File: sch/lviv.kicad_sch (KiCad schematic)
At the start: 0 parts

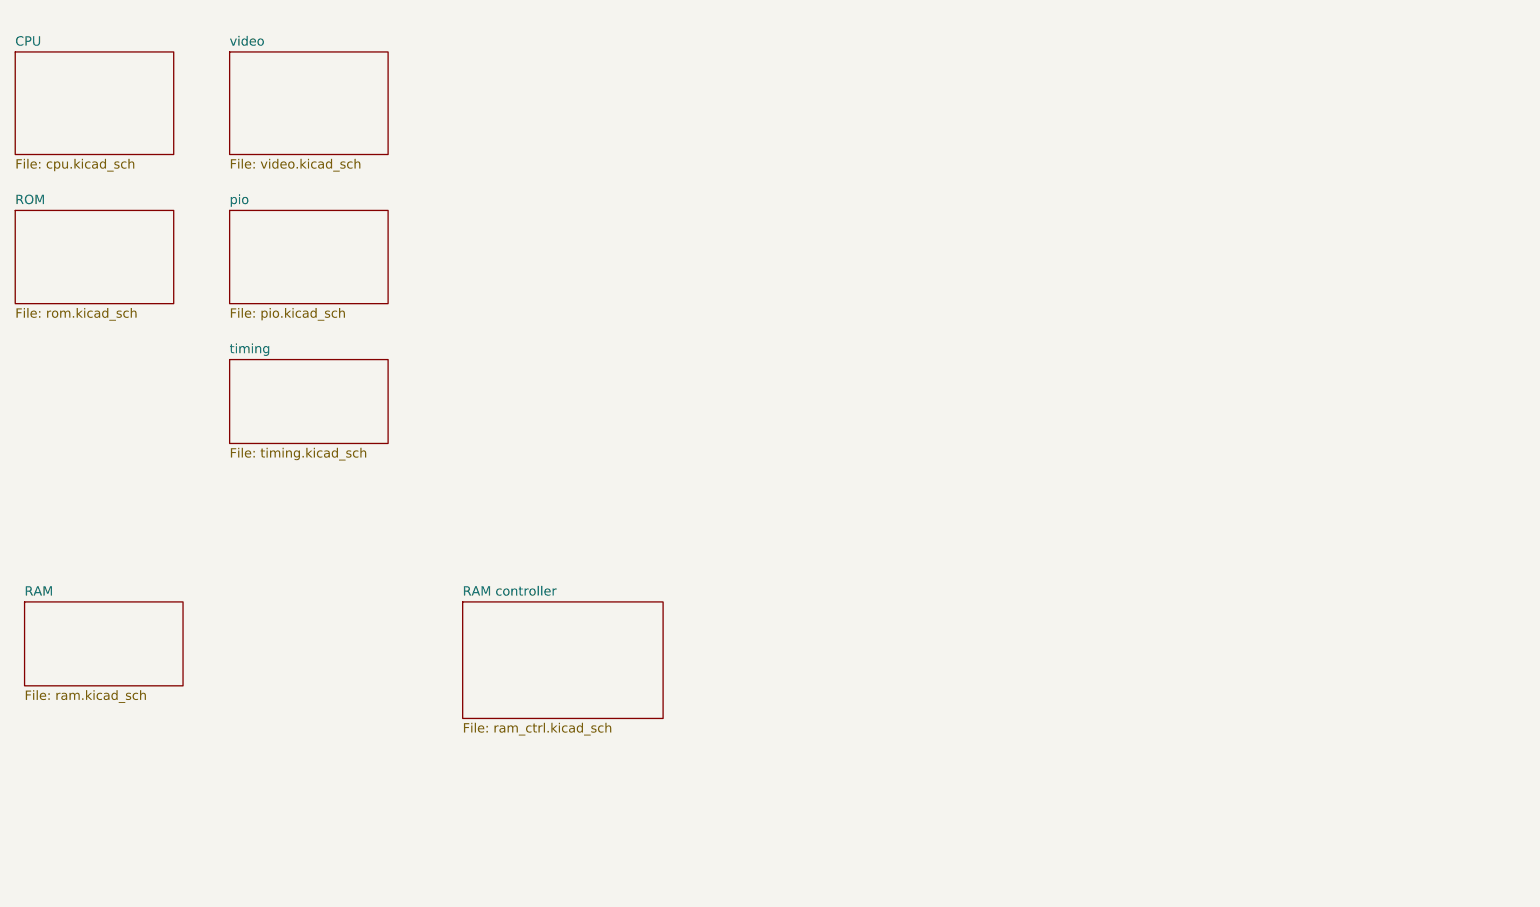
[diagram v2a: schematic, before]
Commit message: Schematics complete
Todo:
- part values
- full review
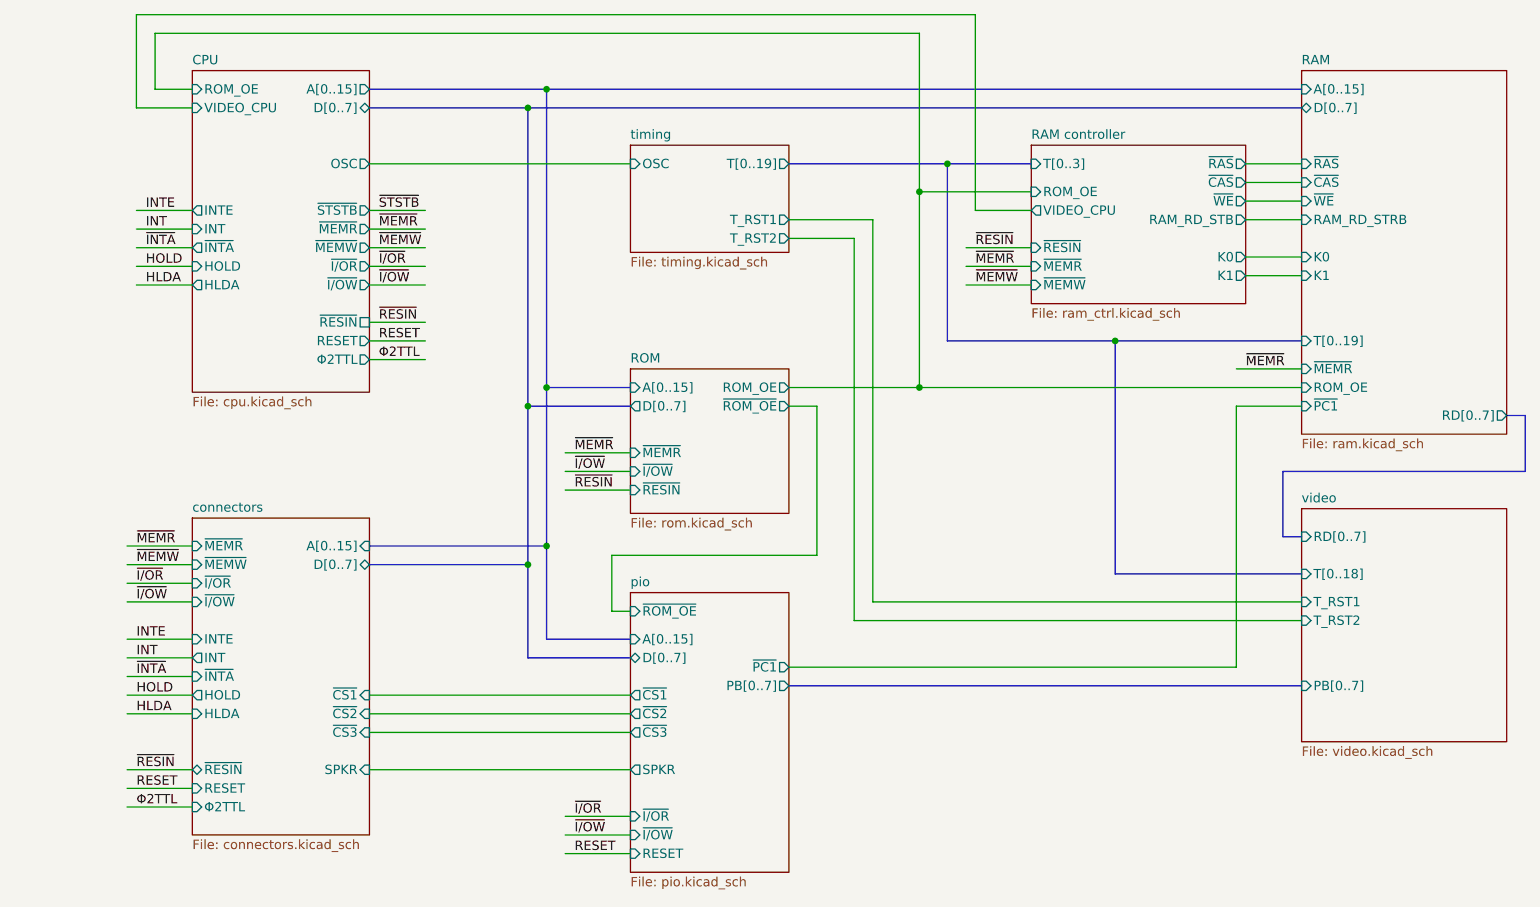
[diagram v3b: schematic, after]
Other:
- added sheet connectors (connectors.kicad_sch)
- sheet CPU ports: added A[0..15], D[0..7], HLDA, HOLD, INT, INTE, OSC, RESET, ROM_OE, VIDEO_CPU, ~{INTA}, ~{I/OR}, ~{I/OW}, ~{MEMR}, ~{MEMW}, ~{RESIN}, ~{STSTB}, Φ2TTL; removed none
- sheet RAM ports: added A[0..15], D[0..7], K0, K1, RAM_RD_STRB, RD[0..7], ROM_OE, T[0..19], ~{CAS}, ~{MEMR}, ~{PC1}, ~{RAS}, ~{WE}; removed none
- sheet RAM controller ports: added K0, K1, RAM_RD_STB, ROM_OE, T[0..3], VIDEO_CPU, ~{CAS}, ~{MEMR}, ~{MEMW}, ~{RAS}, ~{RESIN}, ~{WE}; removed none
- sheet ROM ports: added A[0..15], D[0..7], ROM_OE, ~{I/OW}, ~{MEMR}, ~{RESIN}, ~{ROM_OE}; removed none
- sheet pio ports: added A[0..15], D[0..7], PB[0..7], RESET, SPKR, ~{CS1}, ~{CS2}, ~{CS3}, ~{I/OR}, ~{I/OW}, ~{PC1}, ~{ROM_OE}; removed none
- sheet timing ports: added OSC, T[0..19], T_RST1, T_RST2; removed none
- sheet video ports: added PB[0..7], RD[0..7], T[0..18], T_RST1, T_RST2; removed none
- title: (none) -> Львов ПК-01
